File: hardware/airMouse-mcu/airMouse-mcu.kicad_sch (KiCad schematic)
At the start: 57 parts, among them J1 MCU_PRG, J2 RADIO_PRG, J3 AT, Q1 IRLML6346, SW1 KEY, U1 LSM6DS3TR-C, U2 MCP1640CT-I/CHY, U3 STM32G071RBTx, U4 ESP32-C3-WROOM-02U

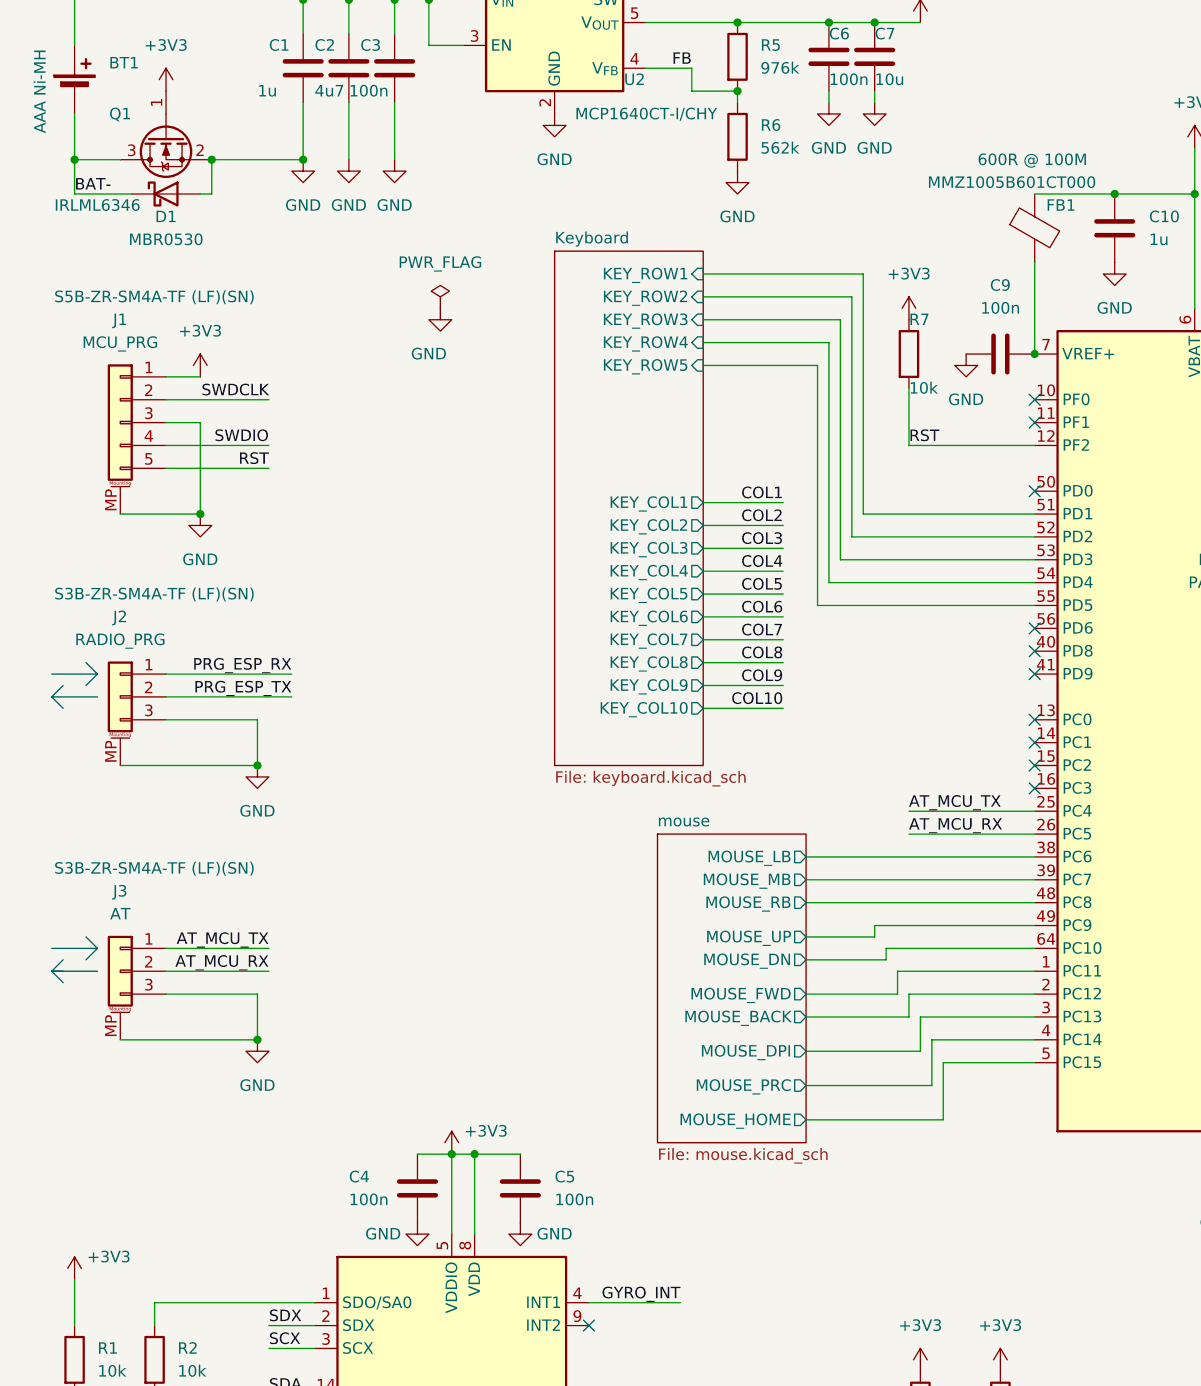
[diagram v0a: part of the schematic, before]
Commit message: fixed home/prc and fwd/bck
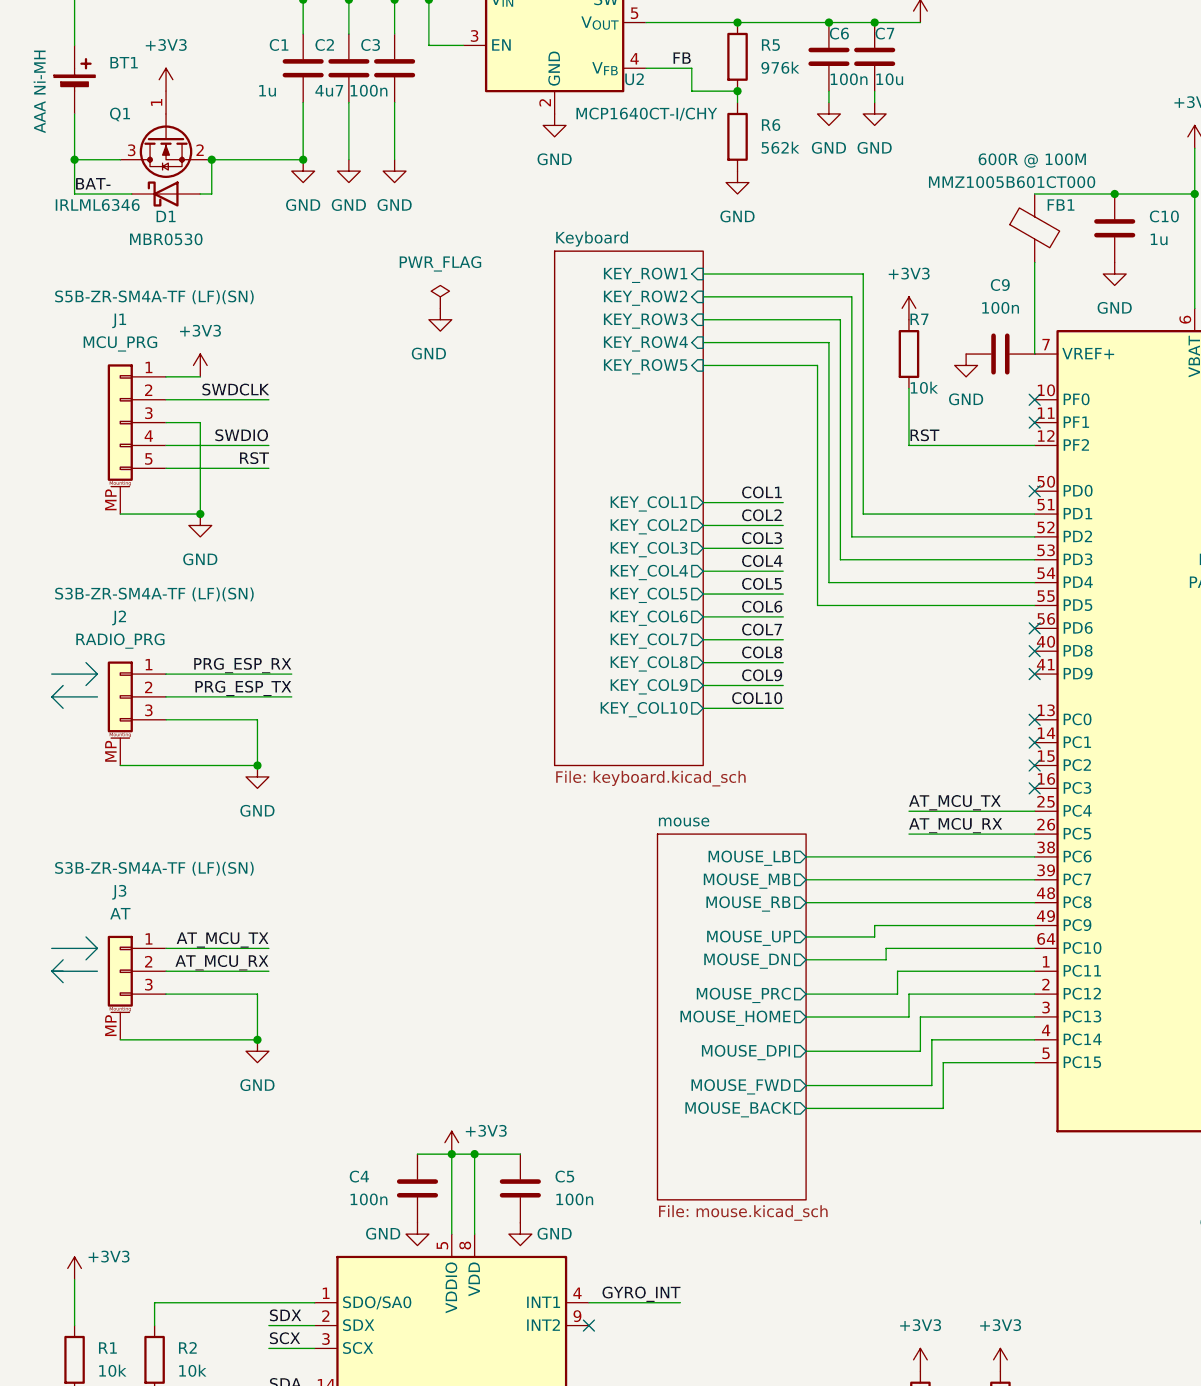
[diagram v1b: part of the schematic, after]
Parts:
- Q1: symbol Device:Q_NMOS_GSD -> Transistor_FET:Q_NMOS_GSD
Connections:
- net mouse/MOUSE_BACK: now also U3.5 (PC15); no longer U3.2 (PC12)
- net mouse/MOUSE_FWD: now also U3.4 (PC14); no longer U3.1 (PC11)
- net mouse/MOUSE_HOME: now also U3.2 (PC12); no longer U3.5 (PC15)
- net mouse/MOUSE_PRC: now also U3.1 (PC11); no longer U3.4 (PC14)
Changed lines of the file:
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@@
 	)
 	(junction
-		(at 124.46 59.69)
-		(diameter 0)
-		(color 0 0 0 0)
-	)
-	(junction
 		(at 57.15 20.32)
 		(diameter 0)
@@
 	(wire
 		(pts
-			(xy 99.06 144.78) (xy 114.3 144.78)
-		)
-		(stroke
-			(width 0)
-			(type default)
-		)
-	)
-	(wire
-		(pts
 			(xy 33.02 38.1) (xy 43.18 38.1)
 		)
@@
 	(wire
 		(pts
+			(xy 99.06 133.35) (xy 110.49 133.35)
+		)
+		(stroke
+			(width 0)
+			(type default)
+		)
+	)
+	(wire
+		(pts
 			(xy 110.49 69.85) (xy 124.46 69.85)
 		)
@@
 	(wire
 		(pts
-			(xy 114.3 144.78) (xy 114.3 138.43)
+			(xy 114.3 143.51) (xy 114.3 138.43)
 		)
 		(stroke
@@
 	(wire
 		(pts
-			(xy 99.06 133.35) (xy 110.49 133.35)
-		)
-		(stroke
-			(width 0)
-			(type default)
-		)
-	)
-	(wire
-		(pts
 			(xy 87.63 81.28) (xy 96.52 81.28)
 		)
@@
 	(wire
 		(pts
-			(xy 99.06 140.97) (xy 113.03 140.97)
-		)
-		(stroke
-			(width 0)
-			(type default)
-		)
-	)
-	(wire
-		(pts
 			(xy 101.6 22.86) (xy 106.68 22.86)
 		)
@@
 		)
 	)
+	(wire
+		(pts
+			(xy 99.06 143.51) (xy 114.3 143.51)
+		)
+		(stroke
+			(width 0)
+			(type default)
+		)
+	)
 	(polyline
 		(pts
@@
 	(wire
 		(pts
+			(xy 99.06 130.81) (xy 109.22 130.81)
+		)
+		(stroke
+			(width 0)
+			(type default)
+		)
+	)
+	(wire
+		(pts
 			(xy 33.02 38.1) (xy 33.02 41.91)
 		)
@@
 	(wire
 		(pts
-			(xy 99.06 130.81) (xy 109.22 130.81)
-		)
-		(stroke
-			(width 0)
-			(type default)
-		)
-	)
-	(wire
-		(pts
 			(xy 101.6 58.42) (xy 101.6 85.09)
 		)
@@
 	(wire
 		(pts
+			(xy 99.06 140.97) (xy 113.03 140.97)
+		)
+		(stroke
+			(width 0)
+			(type default)
+		)
+	)
+	(wire
+		(pts
 			(xy 113.03 140.97) (xy 113.03 135.89)
 		)
@@
 			)
 		)
+		(property "Sim.Pins" "1=K 2=A"
+			(at 200.66 67.31 0)
+			(effects
+				(font
+					(size 1.27 1.27)
+				)
+				(hide yes)
+			)
+		)
 		(pin "2"
 		)
@@
 			)
 		)
+		(property "Sim.Pins" "1=K 2=A"
+			(at 200.66 62.23 0)
+			(effects
+				(font
+					(size 1.27 1.27)
+				)
+				(hide yes)
+			)
+		)
 		(pin "2"
 		)
@@
 			)
 		)
+		(property "Sim.Pins" "1=K 2=A"
+			(at 200.66 72.39 0)
+			(effects
+				(font
+					(size 1.27 1.27)
+				)
+				(hide yes)
+			)
+		)
 		(pin "2"
 		)
@@
 	)
 	(symbol
-		(lib_id "Device:Q_NMOS_GSD")
+		(lib_id "Transistor_FET:Q_NMOS_GSD")
 		(at 27.94 35.56 90)
 		(mirror x)
@@
 	(sheet
 		(at 82.55 113.03)
-		(size 16.51 34.29)
+		(size 16.51 40.64)
 		(exclude_from_sim no)
 		(in_bom yes)
@@
 		)
 		(property "Sheetfile" "mouse.kicad_sch"
-			(at 82.55 147.9046 0)
+			(at 82.55 154.2546 0)
 			(effects
 				(font
@@
 		)
 		(pin "MOUSE_BACK" output
-			(at 99.06 133.35 0)
+			(at 99.06 143.51 0)
 			(effects
 				(font
@@
 		)
 		(pin "MOUSE_HOME" output
-			(at 99.06 144.78 0)
+			(at 99.06 133.35 0)
 			(effects
 				(font
@@
 		)
 		(pin "MOUSE_FWD" output
-			(at 99.06 130.81 0)
+			(at 99.06 140.97 0)
 			(effects
 				(font
@@
 		)
 		(pin "MOUSE_PRC" output
-			(at 99.06 140.97 0)
+			(at 99.06 130.81 0)
 			(effects
 				(font

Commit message: updated for kicad 9
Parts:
- U3: symbol MCU_ST_STM32G0:STM32G071RBTx -> airMouseLib:STM32G071RBT6
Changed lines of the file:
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@@
 	(wire
 		(pts
-			(xy 114.3 143.51) (xy 114.3 138.43)
+			(xy 114.3 144.78) (xy 114.3 138.43)
 		)
 		(stroke
@@
 	(wire
 		(pts
-			(xy 99.06 143.51) (xy 114.3 143.51)
+			(xy 99.06 144.78) (xy 114.3 144.78)
 		)
 		(stroke
@@
 	)
 	(symbol
-		(lib_id "MCU_ST_STM32G0:STM32G071RBTx")
+		(lib_id "airMouseLib:STM32G071RBT6")
 		(at 142.24 102.87 0)
 		(unit 1)
@@
 		(fields_autoplaced yes)
 		(property "Reference" "U3"
-			(at 146.9741 148.59 0)
+			(at 146.9233 148.59 0)
 			(effects
 				(font
@@
 		)
 		(property "Value" "STM32G071RBTx"
-			(at 146.9741 151.13 0)
+			(at 146.9233 151.13 0)
 			(effects
 				(font
@@
 		)
 		(property "Footprint" "Package_QFP:LQFP-64_10x10mm_P0.5mm"
-			(at 127 146.05 0)
+			(at 143.51 97.79 0)
 			(effects
 				(font
 					(size 1.27 1.27)
 				)
-				(justify right)
 				(hide yes)
 			)
@@
 		)
 		(pin "MOUSE_BACK" output
-			(at 99.06 143.51 0)
+			(at 99.06 144.78 0)
 			(effects
 				(font

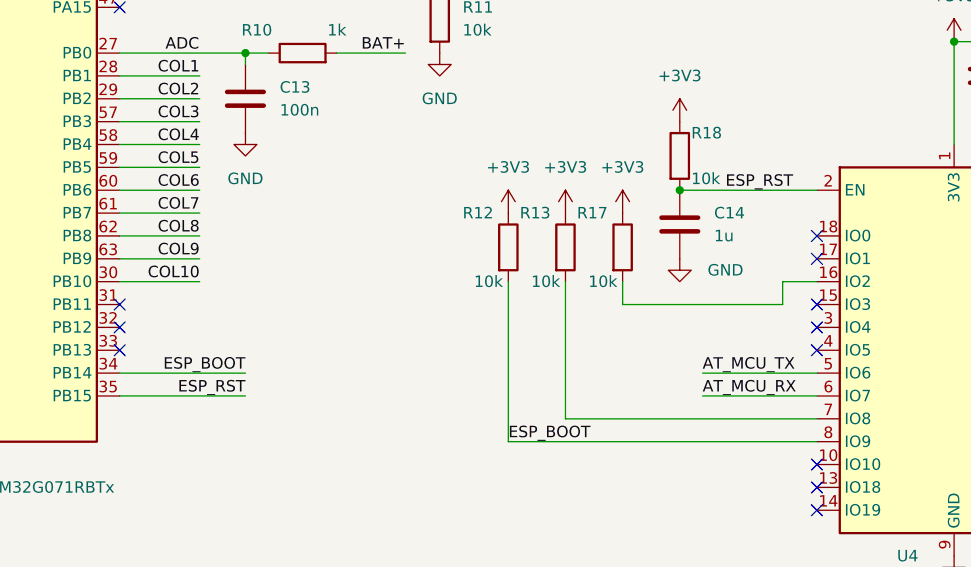
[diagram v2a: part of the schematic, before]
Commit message: dont know, why voltage drops
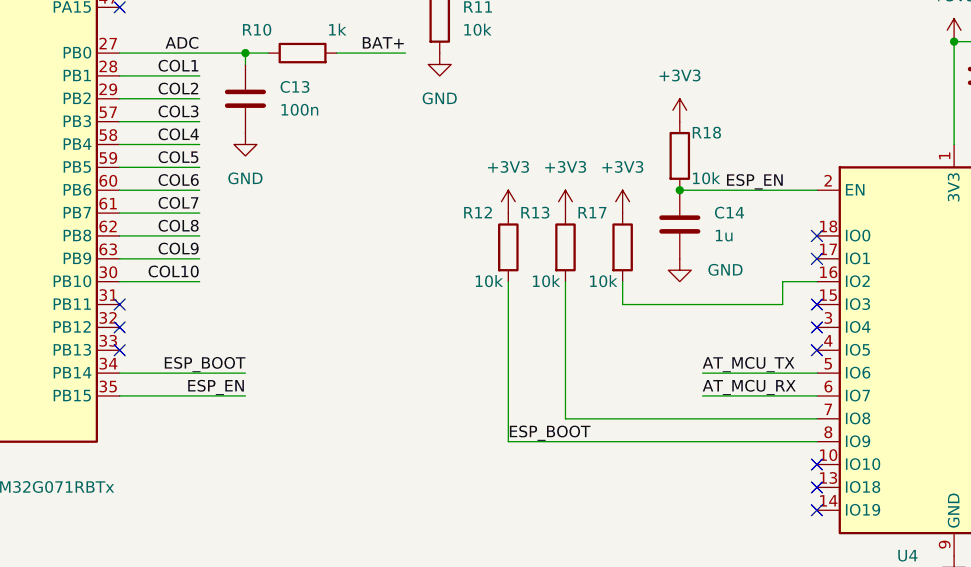
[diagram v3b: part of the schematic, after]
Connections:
- net ESP_RST renamed ESP_EN
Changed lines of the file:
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@@
 		)
 	)
-	(label "ESP_RST"
+	(label "ESP_EN"
 		(at 176.53 140.97 180)
 		(effects
@@
 		)
 	)
-	(label "ESP_RST"
+	(label "ESP_EN"
 		(at 229.87 118.11 0)
 		(effects

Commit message: works with android
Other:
- note added: "remove LASER resistor remove R3/R4 C7- change to 0805 alternative converters: TLV61220 TLV61070A"
- note removed: "usunąć led lasera usunąć R3/R4 C7- zmienić na 0805"
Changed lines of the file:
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@@
 		)
 	)
-	(text "usunąć led lasera\nusunąć R3/R4\nC7- zmienić na 0805"
+	(text "remove LASER resistor\nremove R3/R4\nC7- change to 0805\nalternative converters:\nTLV61220\nTLV61070A"
 		(exclude_from_sim no)
 		(at 326.39 148.59 0)
@@
 				(size 1.27 1.27)
 			)
+			(justify left)
 		)
 	)

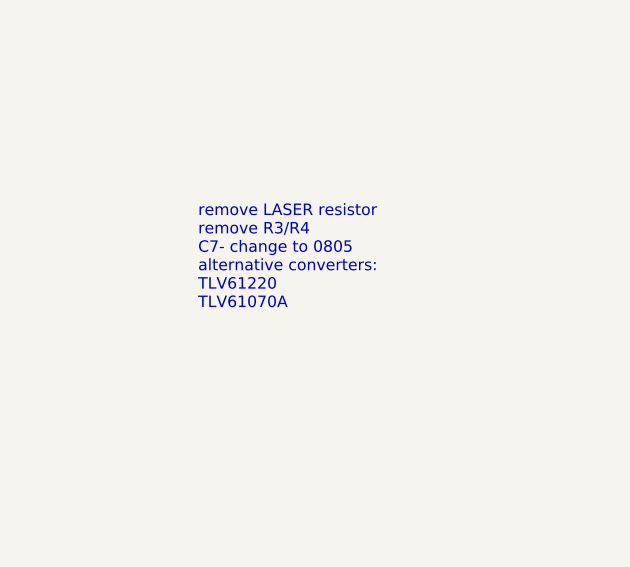
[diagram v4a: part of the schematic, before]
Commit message: created startBoost simulation
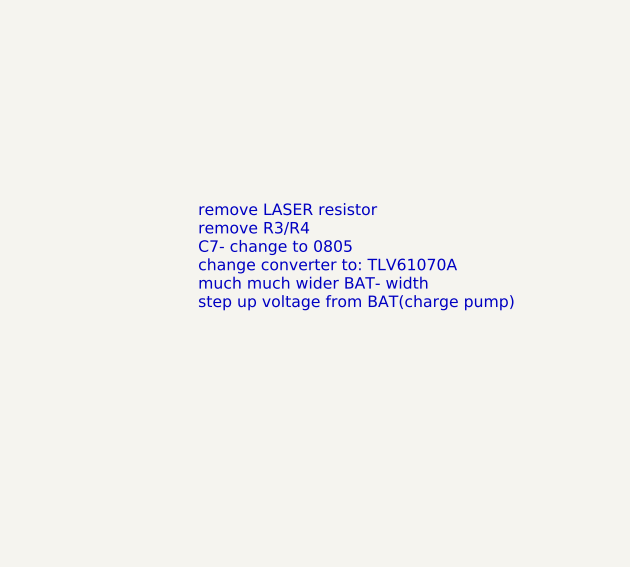
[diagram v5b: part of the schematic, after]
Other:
- note added: "remove LASER resistor remove R3/R4 C7- change to 0805 change converter to: TLV61070A much much wider BAT- width step up voltage from BAT(charge pump)"
- note removed: "remove LASER resistor remove R3/R4 C7- change to 0805 alternative converters: TLV61220 TLV61070A"
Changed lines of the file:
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@@
 		)
 	)
-	(text "remove LASER resistor\nremove R3/R4\nC7- change to 0805\nalternative converters:\nTLV61220\nTLV61070A"
+	(text "remove LASER resistor\nremove R3/R4\nC7- change to 0805\nchange converter to: TLV61070A\nmuch much wider BAT- width\nstep up voltage from BAT(charge pump)"
 		(exclude_from_sim no)
 		(at 326.39 148.59 0)
